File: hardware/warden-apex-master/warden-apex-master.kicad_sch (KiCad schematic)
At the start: 68 parts, among them IC1 SIM7080G, IC2 BQ24650RVAR, IC3 TPS63070RNMR, IC4 MAX98357AETE+T, J1 U.FL-R-SMT-1, J2 U.FL-R-SMT-1, J3 61300211121, Q1 DMG9926UDM, Q2 AO3401A, Q3 2N7002, U1 113991115, U2 Ai-Thinker-Ra-01, U3 M138 Modem, U4 MCP23017_SO, U5 SRV05-4-P-T7, U6 SC16IS740, X1 14.7456MHz

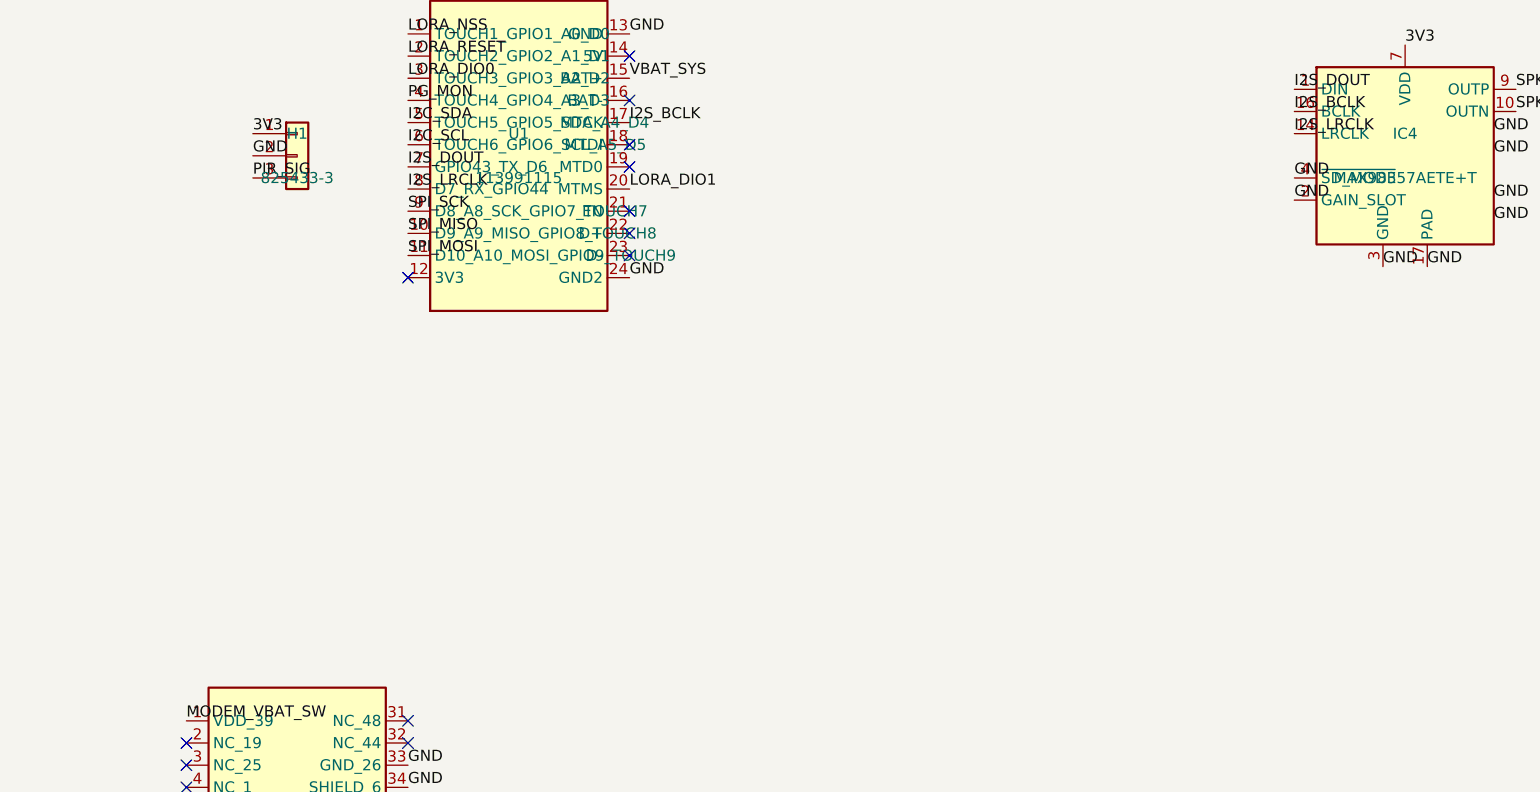
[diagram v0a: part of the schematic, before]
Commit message: Update warden-apex design with new components and net classifications. Added multiple capacitors (C27, C28, C29, C30, C31, C32) and a resistor (R23) to the schematic and PCB. Updated net classes for improved clarity and organization. Adjusted timestamps and documentation in PLAN.md and VARIANTS.md to reflect the latest changes.
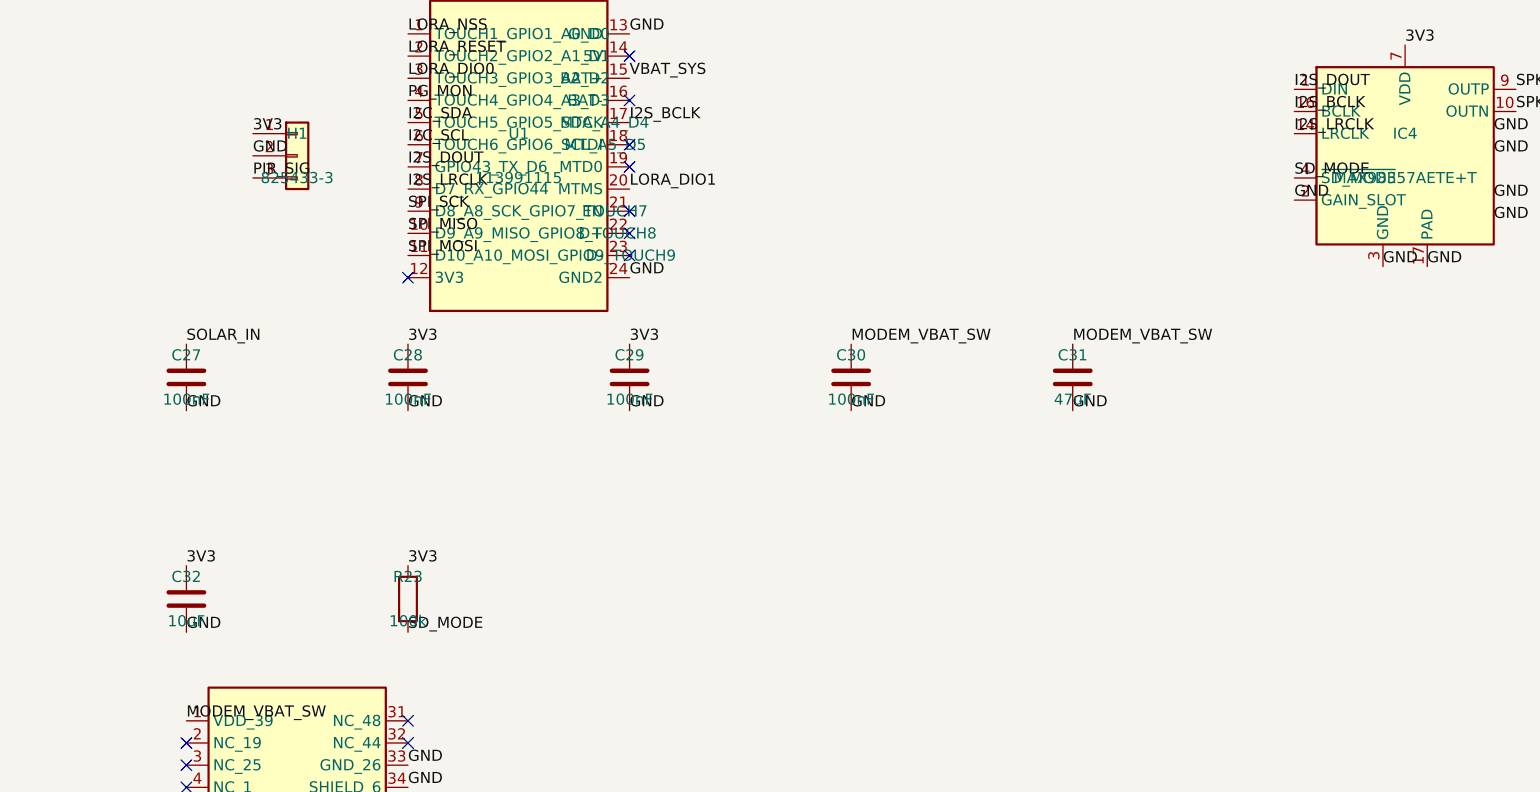
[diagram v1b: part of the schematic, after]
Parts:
- added C27, C28, C29, C30: 100nF, Capacitor_SMD:C_0805_2012Metric, symbol Device:C
- added C31: 47uF, Capacitor_SMD:C_1206_3216Metric, symbol Device:C
- added C32: 10uF, Capacitor_SMD:C_0805_2012Metric, symbol Device:C
- added R23: 100k, Resistor_SMD:R_0805_2012Metric, symbol Device:R
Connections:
- net 3V3: now also C28.1, C29.1, C32.1, R23.1
- net GND: now also C27.2, C28.2, C29.2, C30.2, C31.2, C32.2; no longer IC4.4 (~{SD_MODE})
- net MODEM_VBAT_SW: now also C30.1, C31.1
- net SOLAR_IN: now also C27.1
- new net SD_MODE: IC4.4 (~{SD_MODE}), R23.2

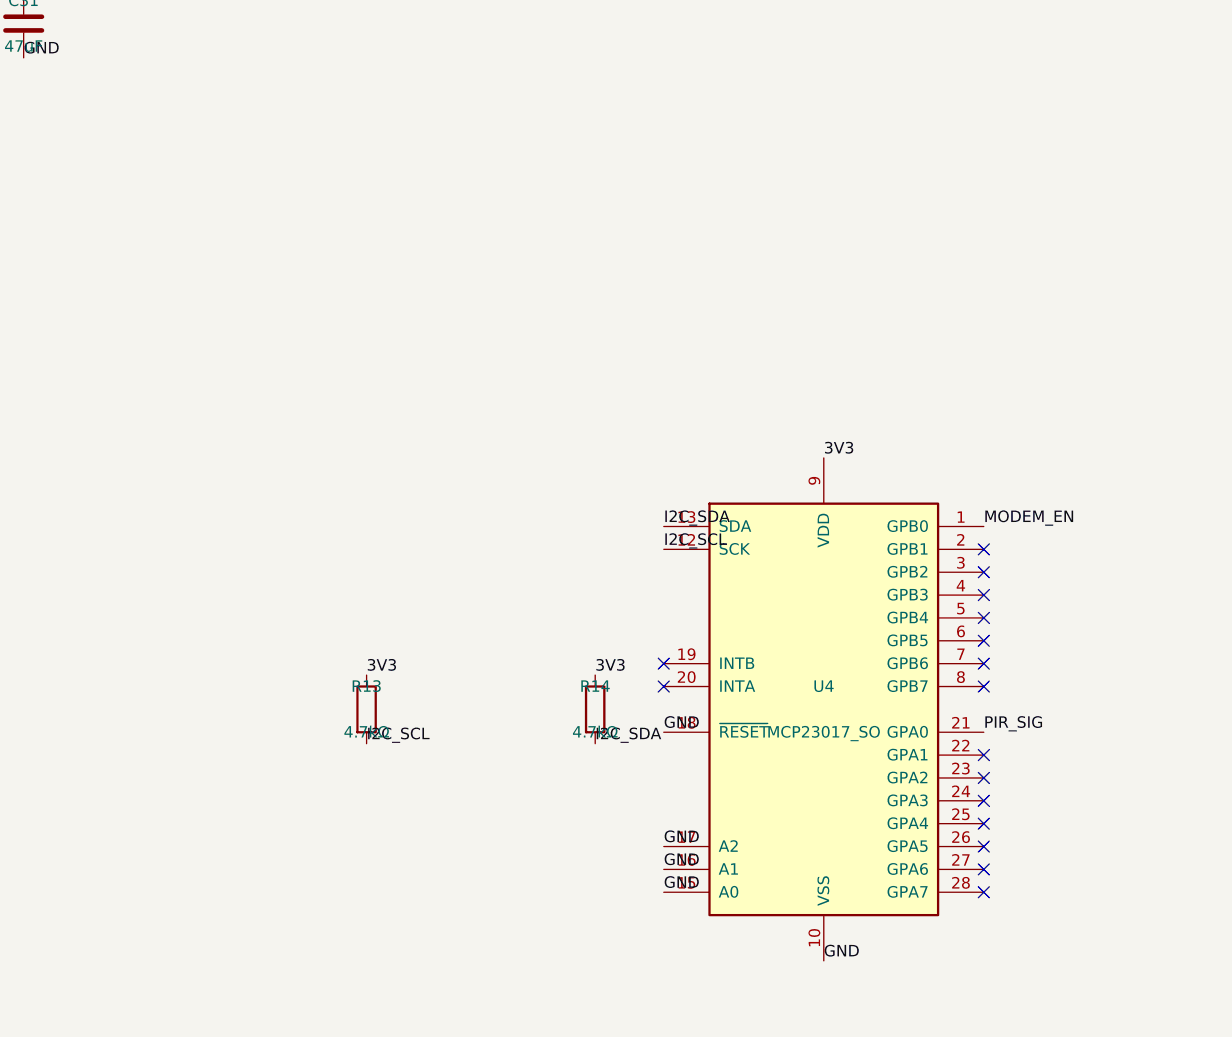
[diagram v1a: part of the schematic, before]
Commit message: Update warden-apex design with new components including F1 (500mA PTC fuse), J4 (Expansion Header), and J5 (Qwiic connector). Adjusted resistor values and footprints for C31 and R24. Updated BOM files and Gerber generation timestamps to reflect the latest changes.
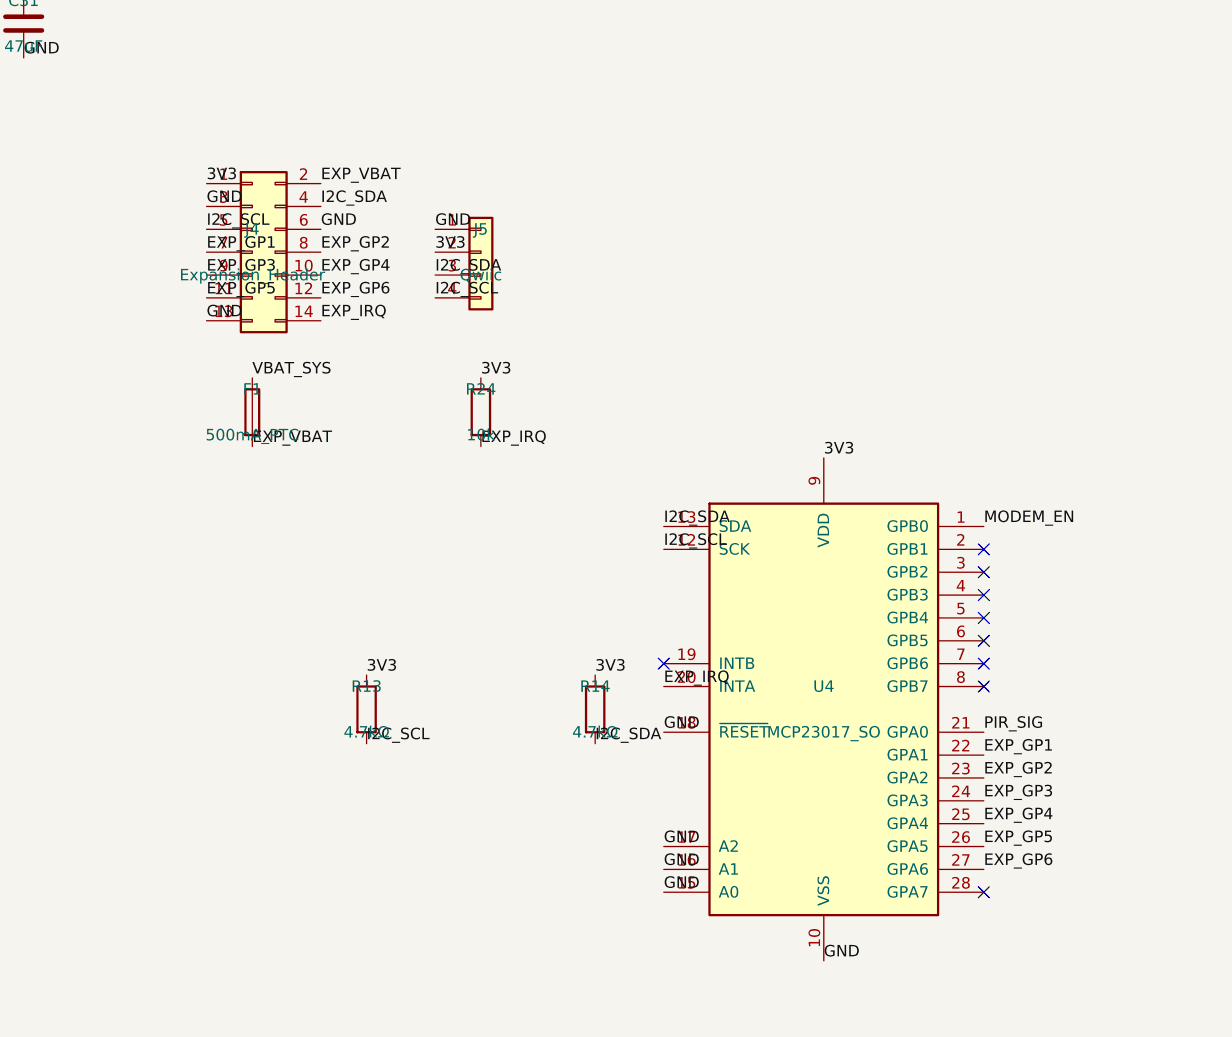
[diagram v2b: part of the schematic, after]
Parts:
- added F1: 500mA_PTC, Fuse:Fuse_0805_2012Metric, symbol Device:Fuse
- added J4: Expansion_Header, Connector_PinHeader_2.54mm:PinHeader_2x07_P2.54mm_Vertical, symbol Connector_Generic:Conn_02x07_Odd_Even
- added J5: Qwiic, Connector_JST:JST_SH_SM04B-SRSS-TB_1x04-1MP_P1.00mm_Horizontal, symbol Connector_Generic:Conn_01x04
- added R24: 10k, Resistor_SMD:R_0805_2012Metric, symbol Device:R
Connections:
- net 3V3: now also J4.1 (Pin_1), J5.2 (Pin_2), R24.1
- net GND: now also J4.13 (Pin_13), J4.3 (Pin_3), J4.6 (Pin_6), J5.1 (Pin_1)
- net I2C_SCL: now also J4.5 (Pin_5), J5.4 (Pin_4)
- net I2C_SDA: now also J4.4 (Pin_4), J5.3 (Pin_3)
- net VBAT_SYS: now also F1.1
- net EXP_IRQ: now reaches U4.20 (INTA)
- net EXP_IRQ: now also J4.14 (Pin_14), R24.2
- net EXP_GP1: now reaches U4.22 (GPA1)
- net EXP_GP1: now also J4.7 (Pin_7)
- net EXP_GP2: now reaches U4.23 (GPA2)
- net EXP_GP2: now also J4.8 (Pin_8)
- net EXP_GP3: now reaches U4.24 (GPA3)
- net EXP_GP3: now also J4.9 (Pin_9)
- net EXP_GP4: now reaches U4.25 (GPA4)
- net EXP_GP4: now also J4.10 (Pin_10)
- net EXP_GP5: now reaches U4.26 (GPA5)
- net EXP_GP5: now also J4.11 (Pin_11)
- net EXP_GP6: now reaches U4.27 (GPA6)
- net EXP_GP6: now also J4.12 (Pin_12)
- new net EXP_VBAT: F1.2, J4.2 (Pin_2)
- no-connect marks 112 -> 105

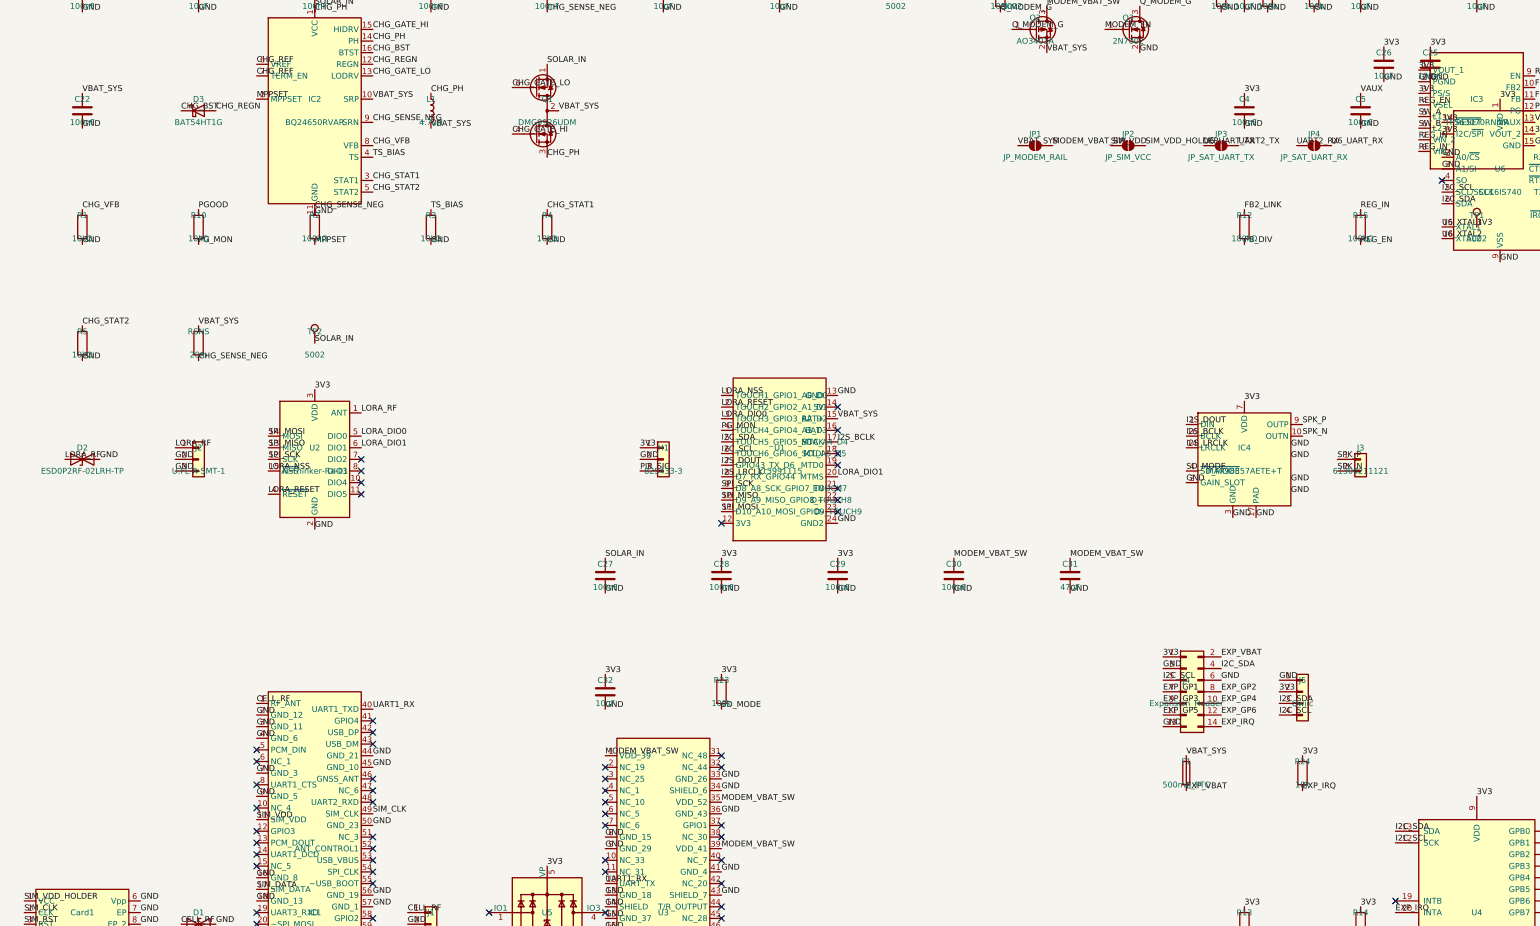
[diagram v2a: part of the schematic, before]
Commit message: Update warden-apex design with new resistor values and components. Changed C5 to 1uF and added resistors R20 (7.15k) and R21 (10k) to the schematic. Updated BOM files to reflect these changes and adjusted Gerber generation timestamps for consistency.
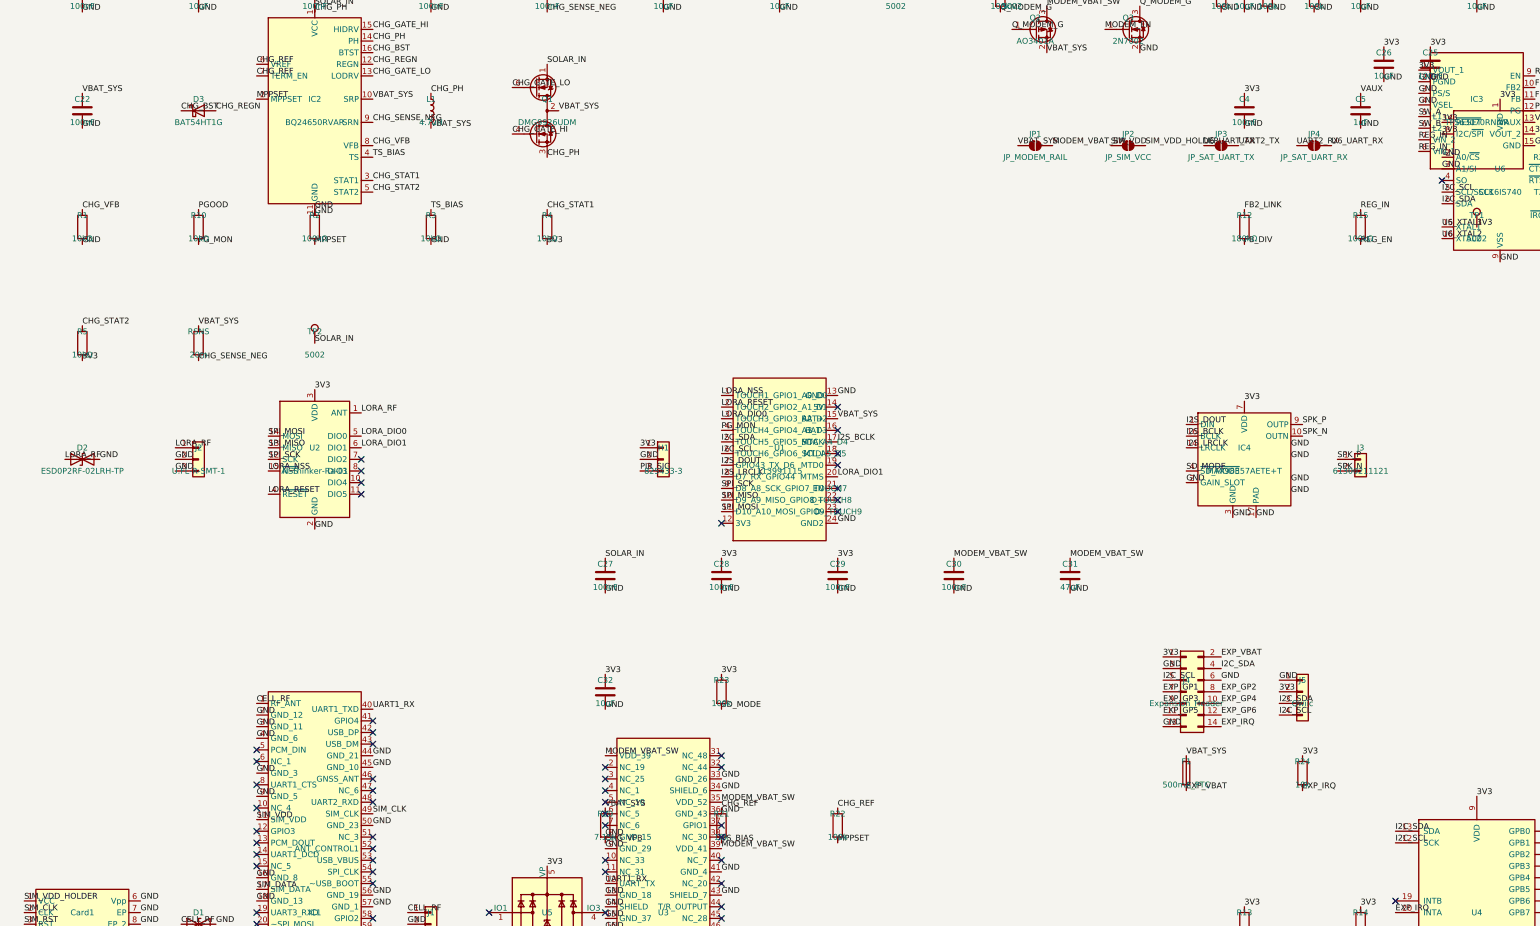
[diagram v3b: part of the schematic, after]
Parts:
- added R20: 7.15k, Resistor_SMD:R_0805_2012Metric, symbol Device:R
- added R21: 10k, Resistor_SMD:R_0805_2012Metric, symbol Device:R
- added R22: 100k, Resistor_SMD:R_0805_2012Metric, symbol Device:R
- C5: value 100nF -> 1uF
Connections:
- net 3V3: now also R4.2, R5.2; no longer IC3.3 (PS/S)
- net CHG_REF: now also R21.1, R22.1
- net CHG_SENSE_NEG: no longer R2.1
- net CHG_VFB: now also R20.2
- net GND: now also IC3.3 (PS/S), IC3.4 (VSEL), R2.1; no longer R4.2, R5.2
- net MPPSET: now also R22.2
- net REG_EN: no longer IC3.4 (VSEL)
- net TS_BIAS: now also R21.2
- net VBAT_SYS: now also R20.1
